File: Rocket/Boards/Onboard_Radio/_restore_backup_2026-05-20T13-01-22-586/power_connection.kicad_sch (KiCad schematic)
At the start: 1 part, among them J5 Conn_01x08

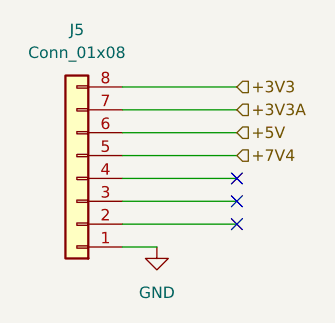
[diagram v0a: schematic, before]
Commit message: schematic bom needs updating and traces need finishing
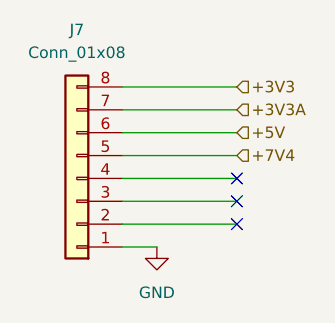
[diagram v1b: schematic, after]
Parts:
- J7: renamed from J5; footprint Connector_PinSocket_2.54mm:PinSocket_1x08_P2.54mm_Vertical -> (none)
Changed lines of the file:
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@@
 		(dnp no)
 		(fields_autoplaced yes)
-		(property "Reference" "J5"
+		(property "Reference" "J7"
 			(at 125.73 80.01 0)
 			(show_name no)
@@
 			)
 		)
-		(property "Footprint" "Connector_PinSocket_2.54mm:PinSocket_1x08_P2.54mm_Vertical"
+		(property "Footprint" ""
 			(at 125.73 96.52 0)
 			(hide yes)
@@
 			(project "rf_rocket_module"
 				(path "/4940ffbe-f45f-4917-a247-12e2b32b6c35/abcae1e2-b29e-4289-bda9-47e90da98056"
-					(reference "J5")
+					(reference "J7")
 					(unit 1)
 				)
